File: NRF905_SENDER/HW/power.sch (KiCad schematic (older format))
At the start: 11 parts, among them Q1 IRLML6402

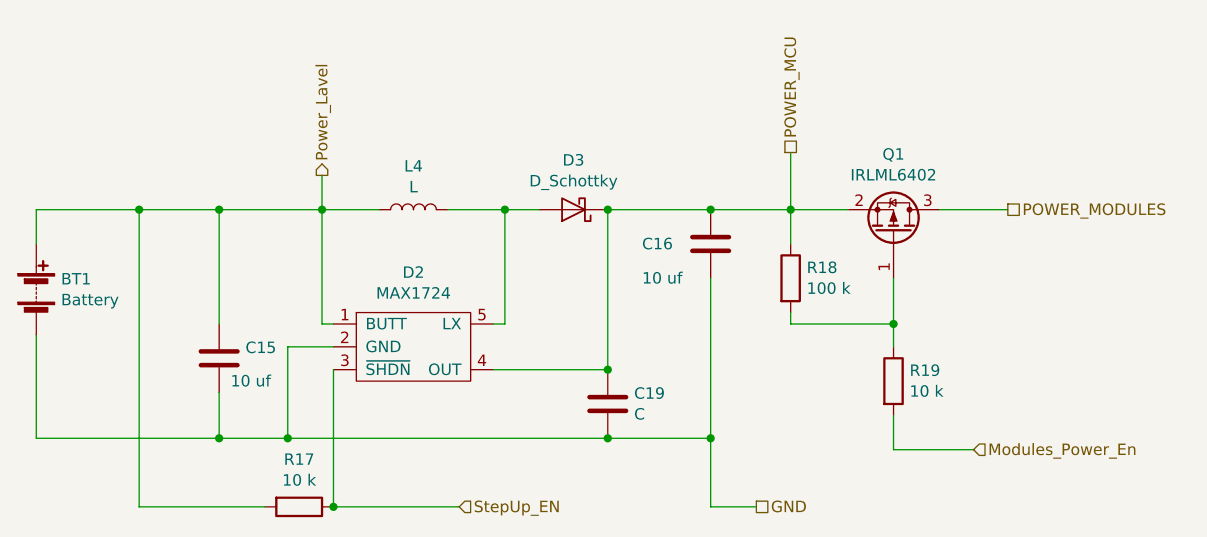
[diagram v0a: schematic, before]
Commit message: Изменена структура проека. Добавлен шаблон проекта для ESP32. Изменение в схемотехнике WIFI модуль с ESP-07 изменени на ESP32 WROVER-IB
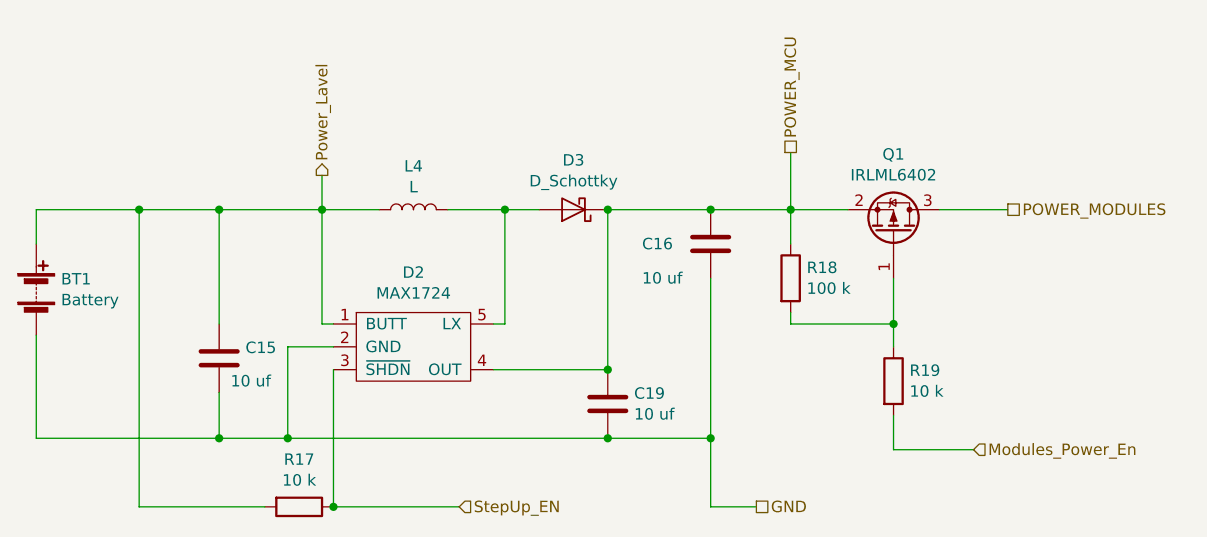
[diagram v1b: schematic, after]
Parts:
- C19: value C -> 10 uf
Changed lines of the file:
@@
 P 6550 3650
 F 0 "C19" H 6665 3696 50  0000 L CNN
-F 1 "C" H 6665 3605 50  0000 L CNN
+F 1 "10 uf" H 6665 3605 50  0000 L CNN
 F 2 "Capacitor_SMD:C_0603_1608Metric" H 6588 3500 50  0001 C CNN
 F 3 "~" H 6550 3650 50  0001 C CNN
